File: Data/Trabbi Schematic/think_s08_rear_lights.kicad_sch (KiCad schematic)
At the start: 11 parts, among them K1 Reverse Light Relay R7, SW1 Brake Light Switch (C12)

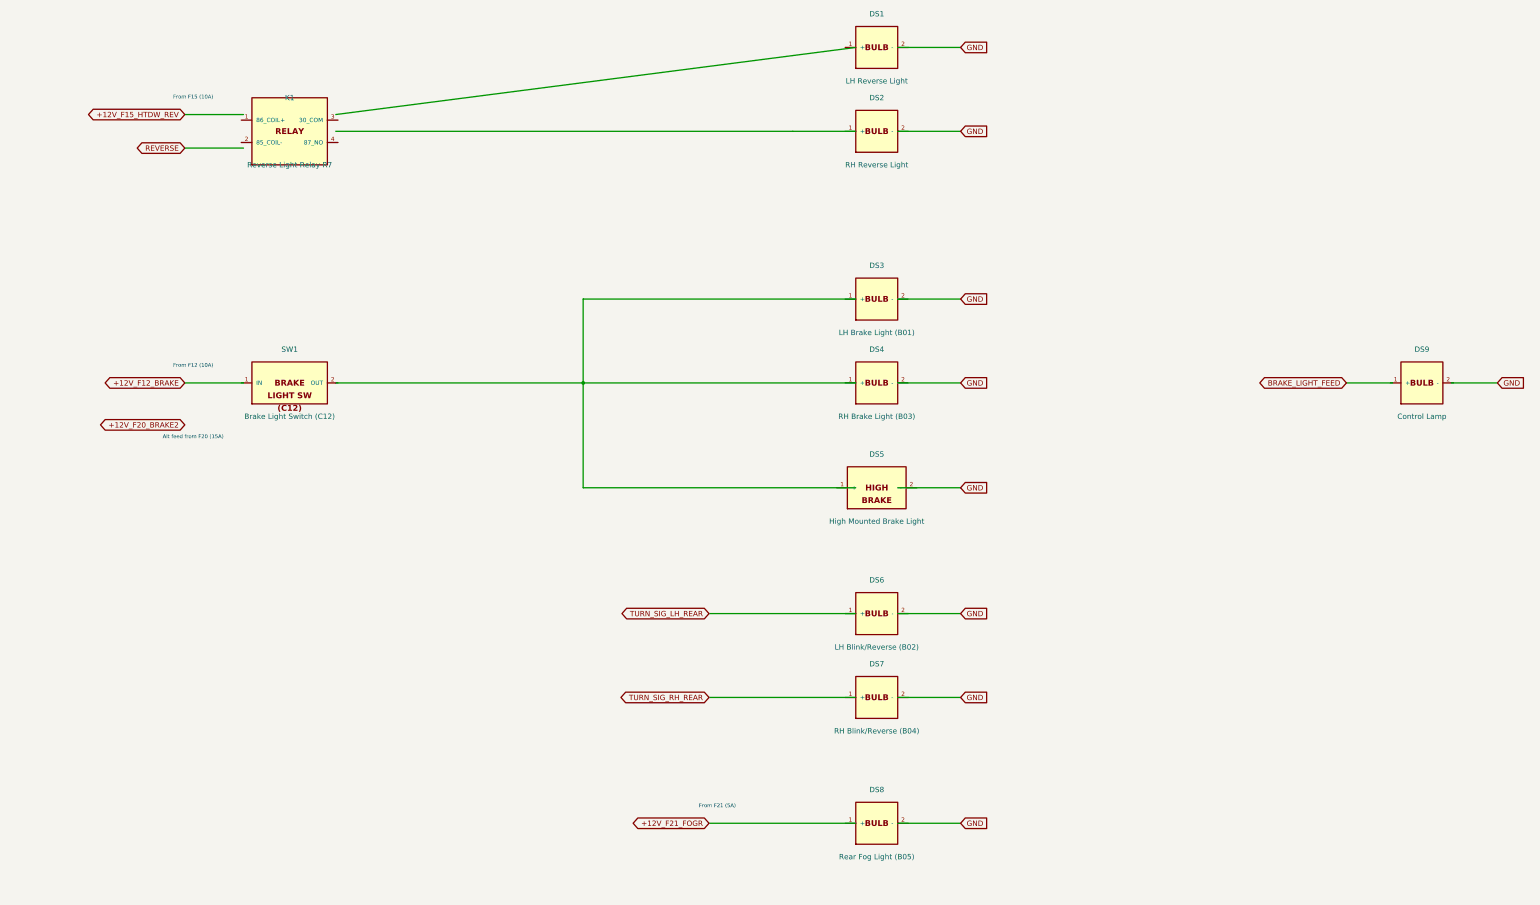
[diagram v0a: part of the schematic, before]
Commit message: Fix wire-to-pin connections: use exact calculated pin positions
Refactored gen_think_complete.py to compute exact pin schematic
coordinates instead of using approximate manual offsets. Added p()
method to Sheet class that transforms symbol-local pin positions to
schematic coordinates. All 232 wire calls across 13 sub-sheet
generators now use p() for pin endpoints, fixing misaligned
connections (previously off by 0.54-10+ units).

Co-Authored-By: Claude Opus 4.6 <noreply@anthropic.com>
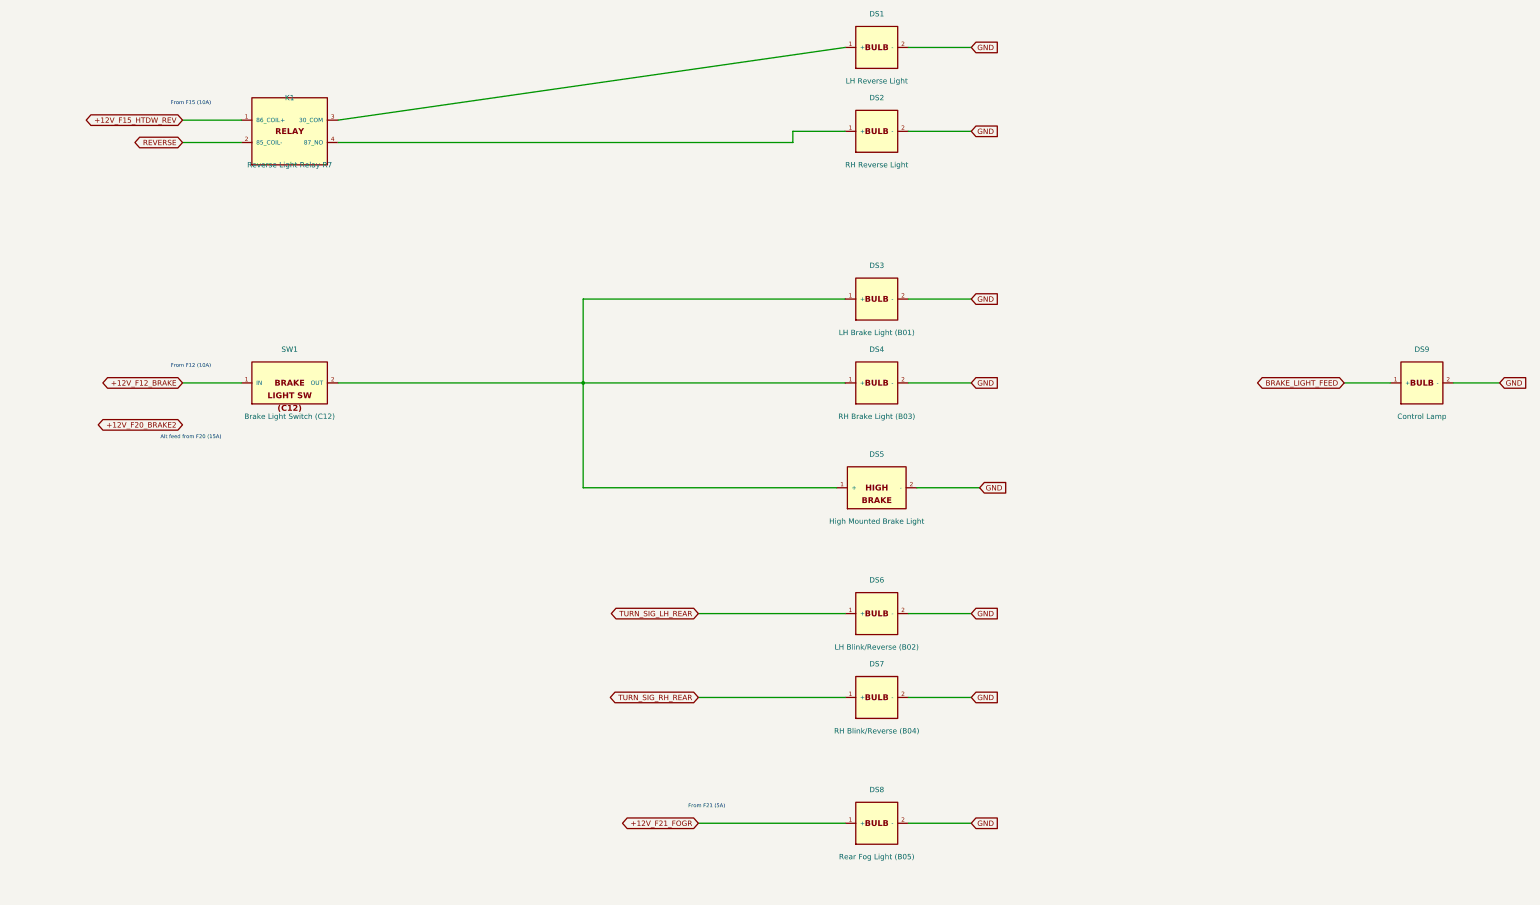
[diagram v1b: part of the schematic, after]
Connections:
- net +12V_F12_BRAKE: now also SW1.1 (IN)
- net +12V_F15_HTDW_REV: now also K1.1 (86_COIL+)
- net +12V_F21_FOGR: now also DS8.1 (+)
- net BRAKE_LIGHT_FEED: now also DS9.1 (+)
- net GND: now also DS1.2 (-), DS2.2 (-), DS3.2 (-), DS4.2 (-), DS5.2 (-), DS6.2 (-), DS7.2 (-), DS8.2 (-), DS9.2 (-)
- net REVERSE: now also K1.2 (85_COIL-)
- net TURN_SIG_LH_REAR: now also DS6.1 (+)
- net TURN_SIG_RH_REAR: now also DS7.1 (+)
- net at DS3.1 (+): now also DS4.1 (+), DS5.1 (+), SW1.2 (OUT)
- net at K1.3 (30_COM): now also DS1.1 (+)
- net at K1.4 (87_NO): now also DS2.1 (+)

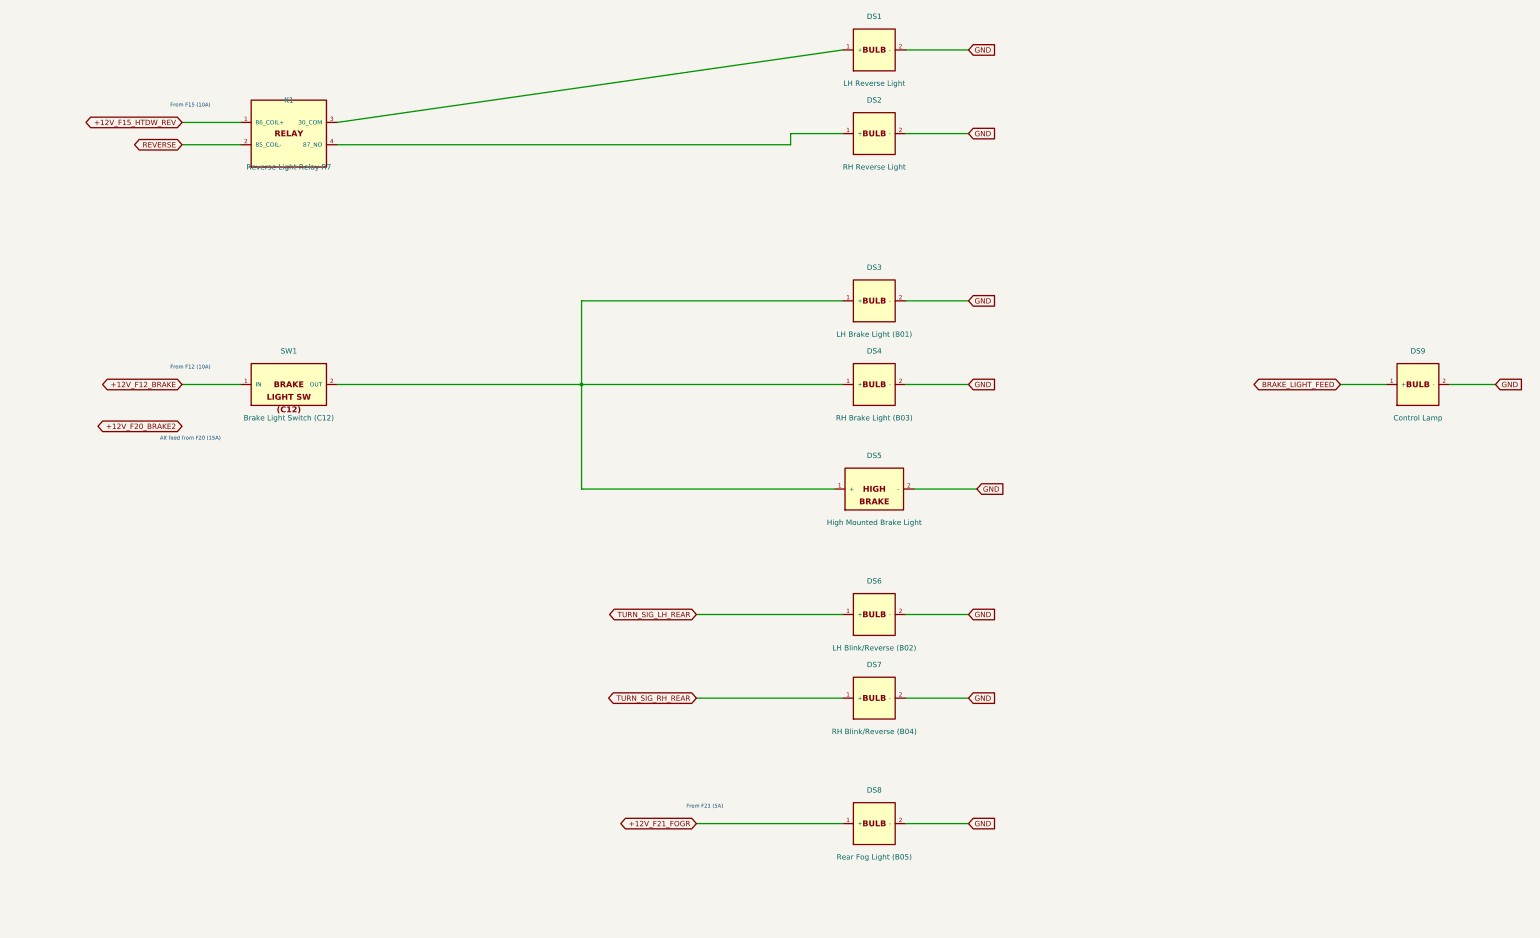
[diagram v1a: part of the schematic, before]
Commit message: Enforce orthogonal routing and 1.27mm grid alignment
- Add _g() grid snap function to Sheet class (rounds all coordinates to nearest 1.27mm)
- Add wire_l() method for L-shaped orthogonal routing (horizontal+vertical segments)
- Apply grid snapping in p(), place(), wire(), label(), glabel(), junction(), no_connect(), defsym()
- Replace all 19 diagonal wire calls with wire_l() across S02, S06, S07, S08, S10, S12, S13
- All wire segments now strictly horizontal or vertical, no diagonals
- All coordinates verified on 1.27mm (50mil) KiCad standard grid

Co-Authored-By: Claude Opus 4.6 <noreply@anthropic.com>
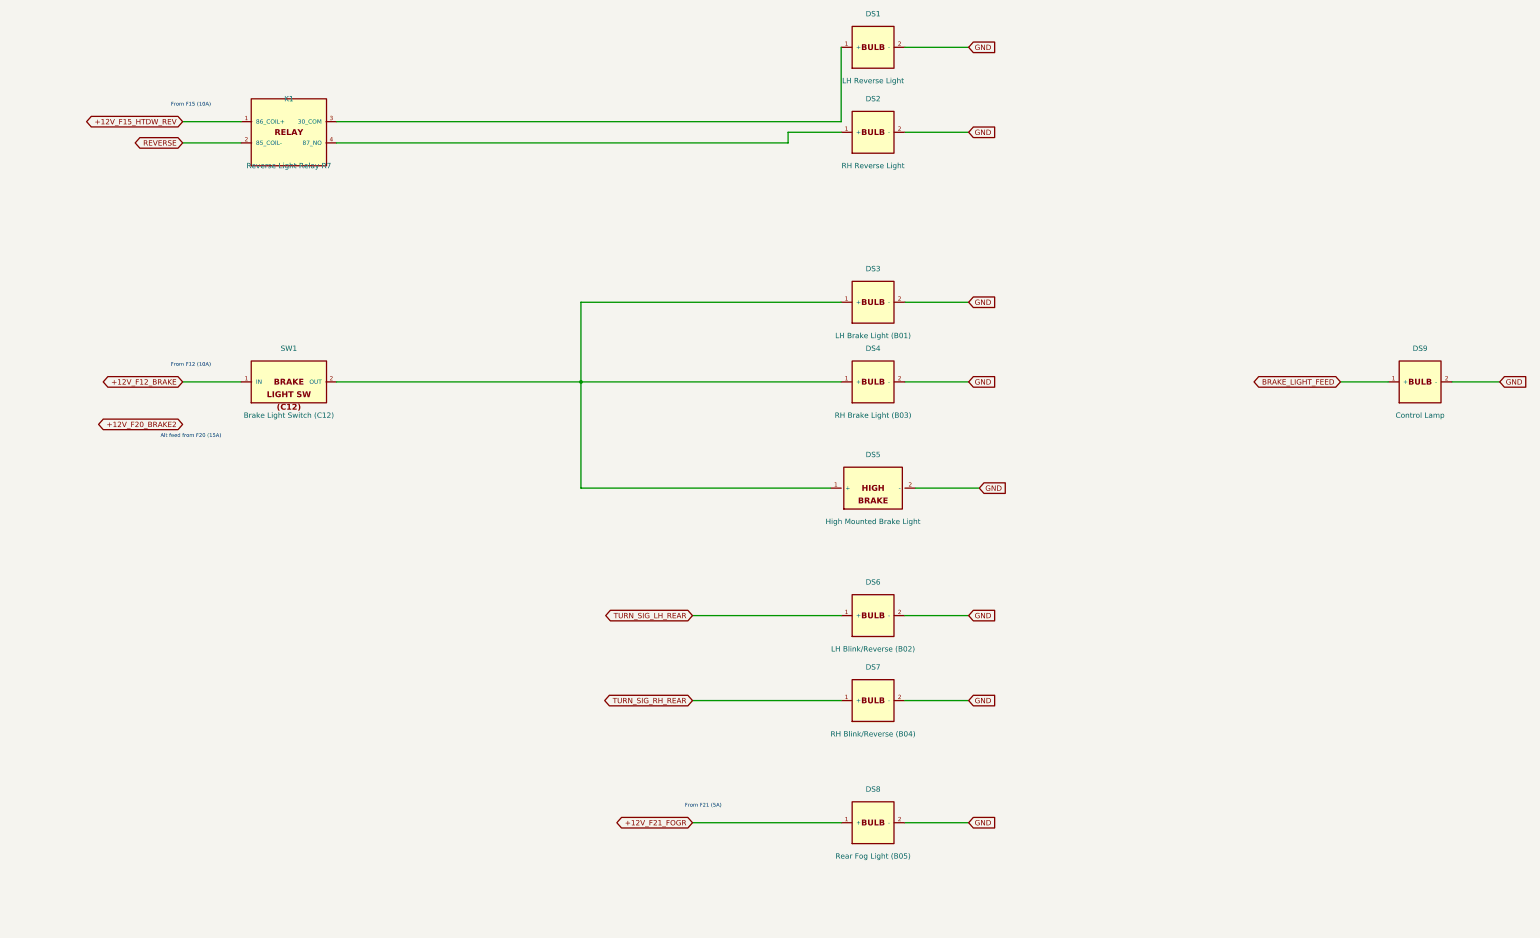
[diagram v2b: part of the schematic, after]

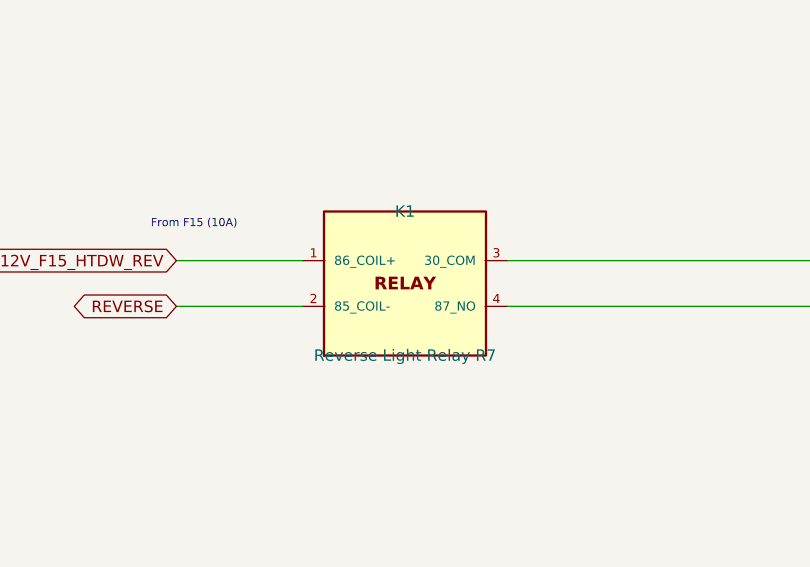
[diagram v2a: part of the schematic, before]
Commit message: Add relay coil/switch graphics, fix label positioning
- Draw coil (inductor arcs) and switch contacts (circles + arm)
  inside RELAY_SPST and RELAY_SPDT symbol bodies
- Add body_gfx parameter to defsym() for custom symbol graphics
- Helper functions: _gfx_polyline, _gfx_arc, _gfx_circle, _relay_gfx
- Fix label offsets: increase from 3-5mm to 10-12mm to avoid
  overlapping pin names (S01 ignition, S02 HV, S05 DCDC, S07 lights)
- Fix S09 turn signal rear labels: add wire stubs (were at 0 offset)
- All 14 schematics regenerated, parentheses balanced, grid OK

Co-Authored-By: Claude Opus 4.6 <noreply@anthropic.com>
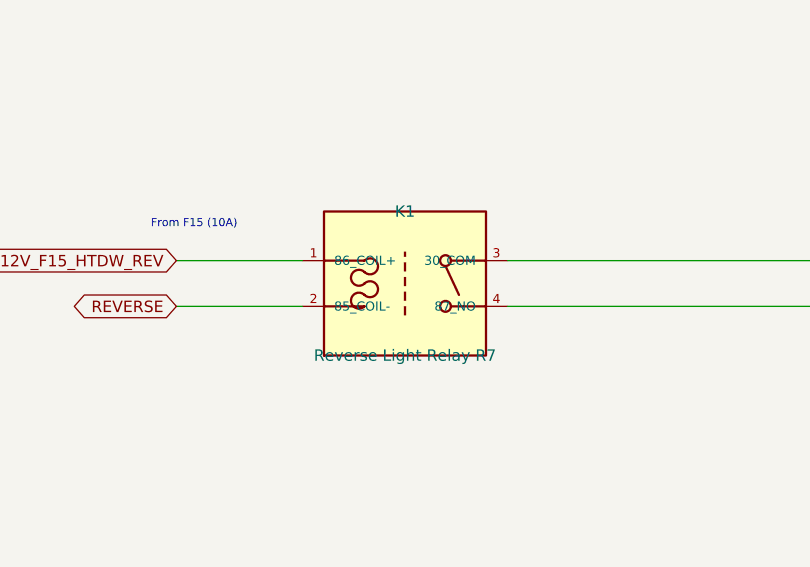
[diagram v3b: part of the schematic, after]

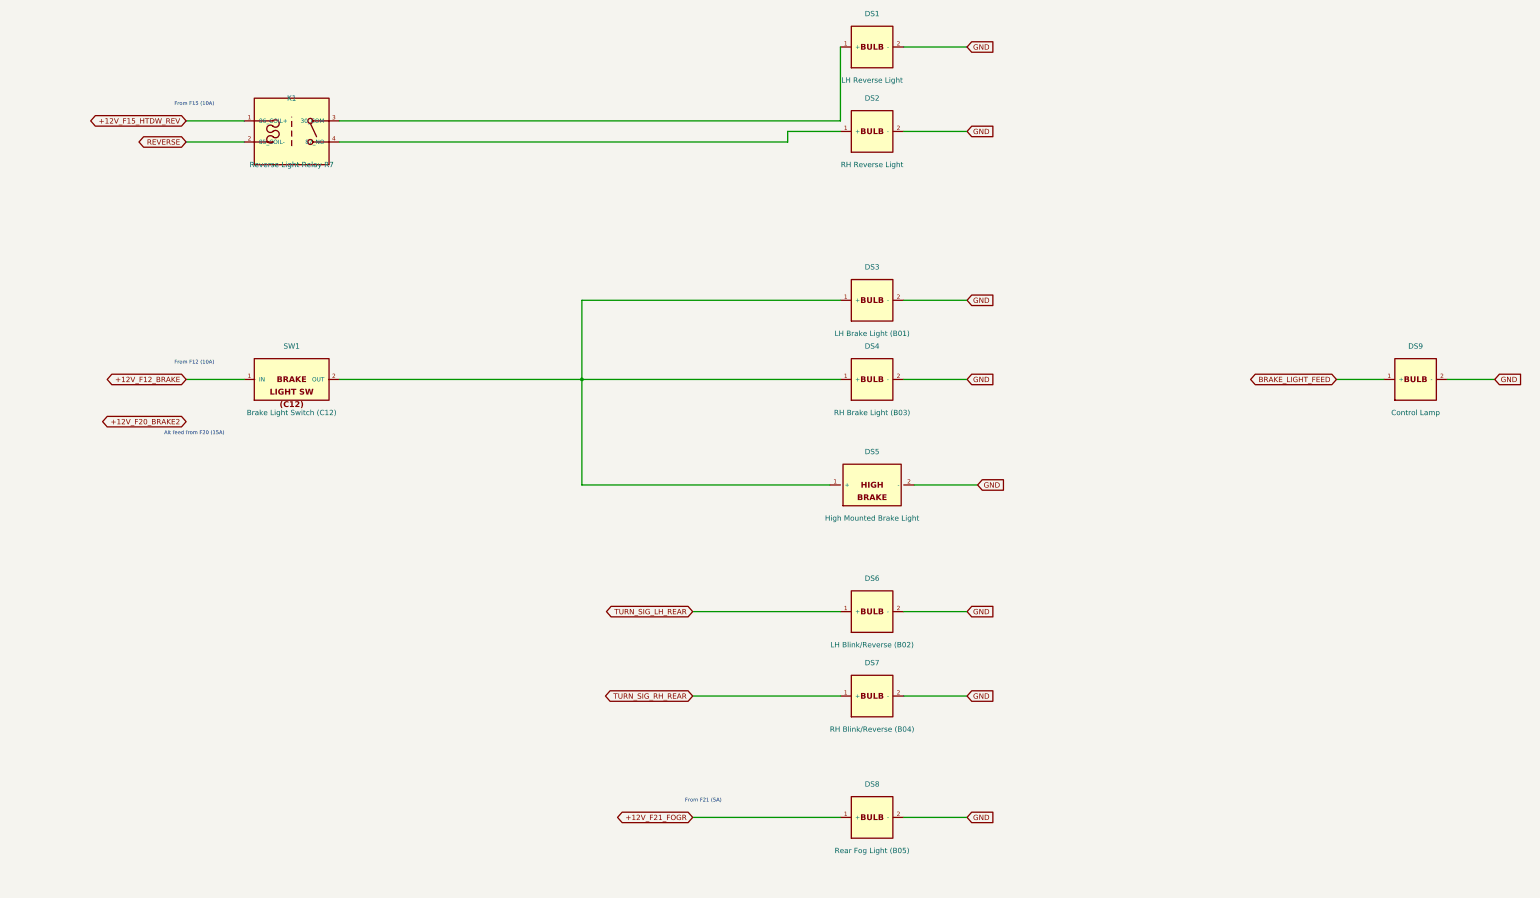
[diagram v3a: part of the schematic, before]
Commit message: Fix label/text positioning: Ref/Value outside body, hide pin numbers
- Reference placed above body edge, Value below (dynamic based on
  symbol height) — no longer overlapping body text
- Pin numbers hidden (clutter, not useful in schematic view)
- Pin name font reduced from 1.016mm to 0.762mm (less overlap)
- Pin length increased from 2.54mm to 3.81mm (more room for pin names
  between body edge and endpoint)
- Store symbol dimensions in _sym_dims for dynamic property placement

Co-Authored-By: Claude Opus 4.6 <noreply@anthropic.com>
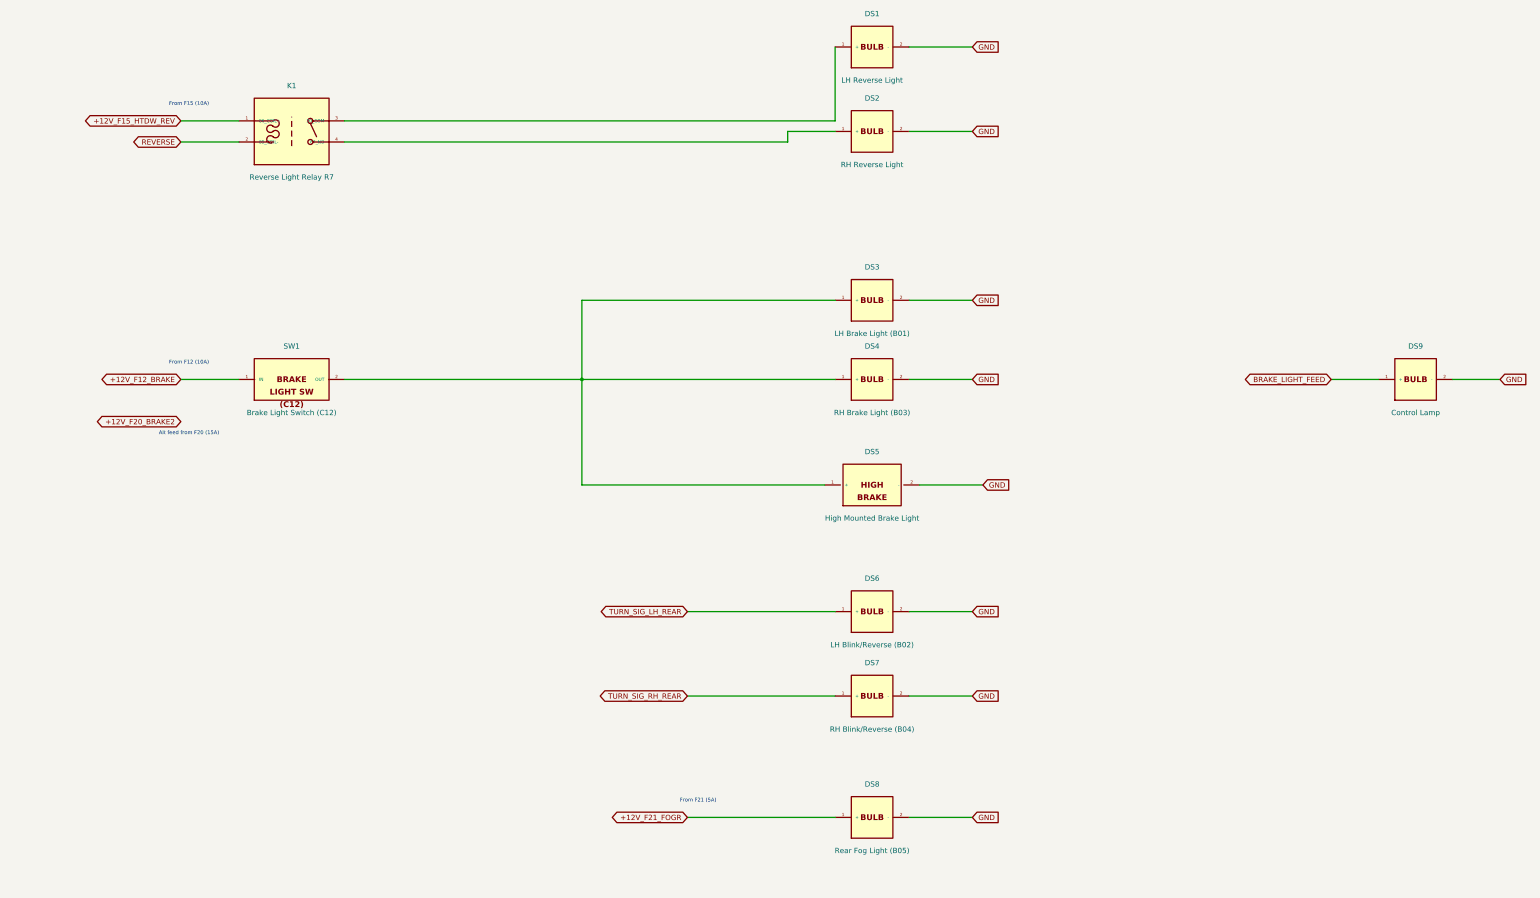
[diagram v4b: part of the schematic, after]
